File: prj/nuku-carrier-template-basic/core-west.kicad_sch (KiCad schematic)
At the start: 1 part, among them J4 DF40HC(4.0)-90DS-0.4V

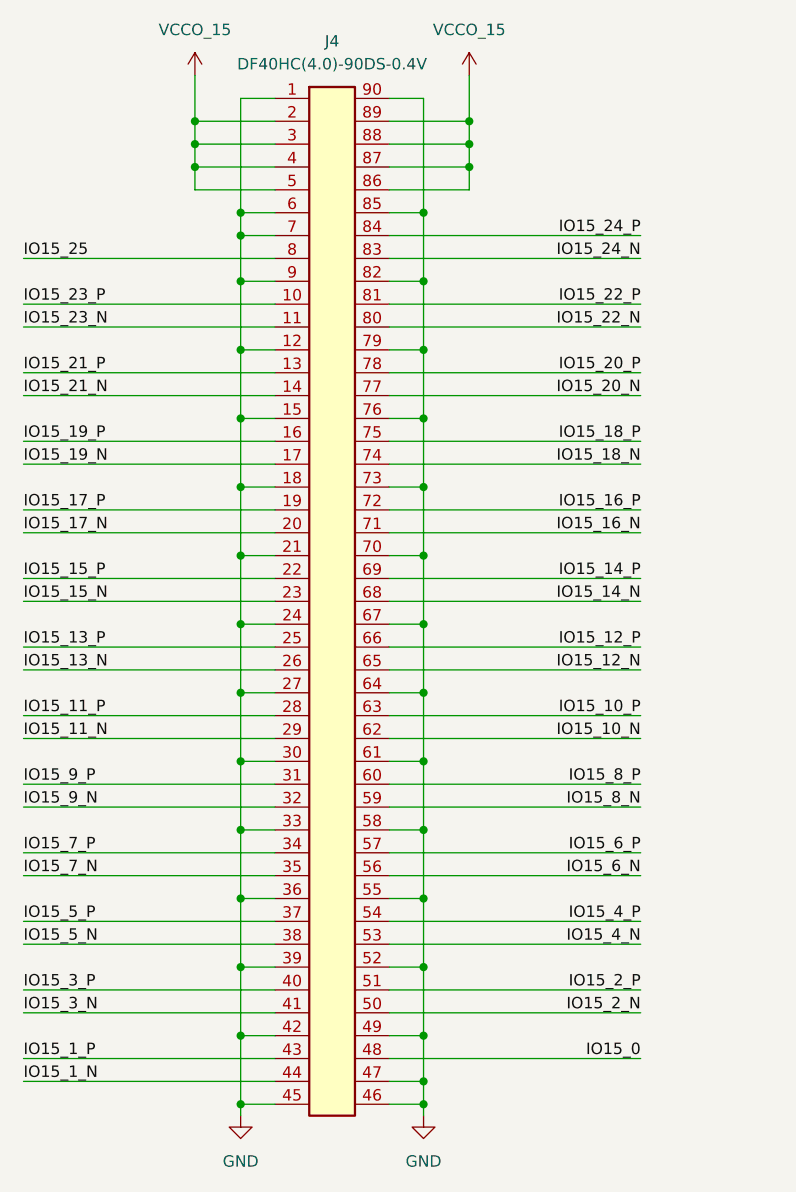
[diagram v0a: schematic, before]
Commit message: Finish template.basic + Production outputs
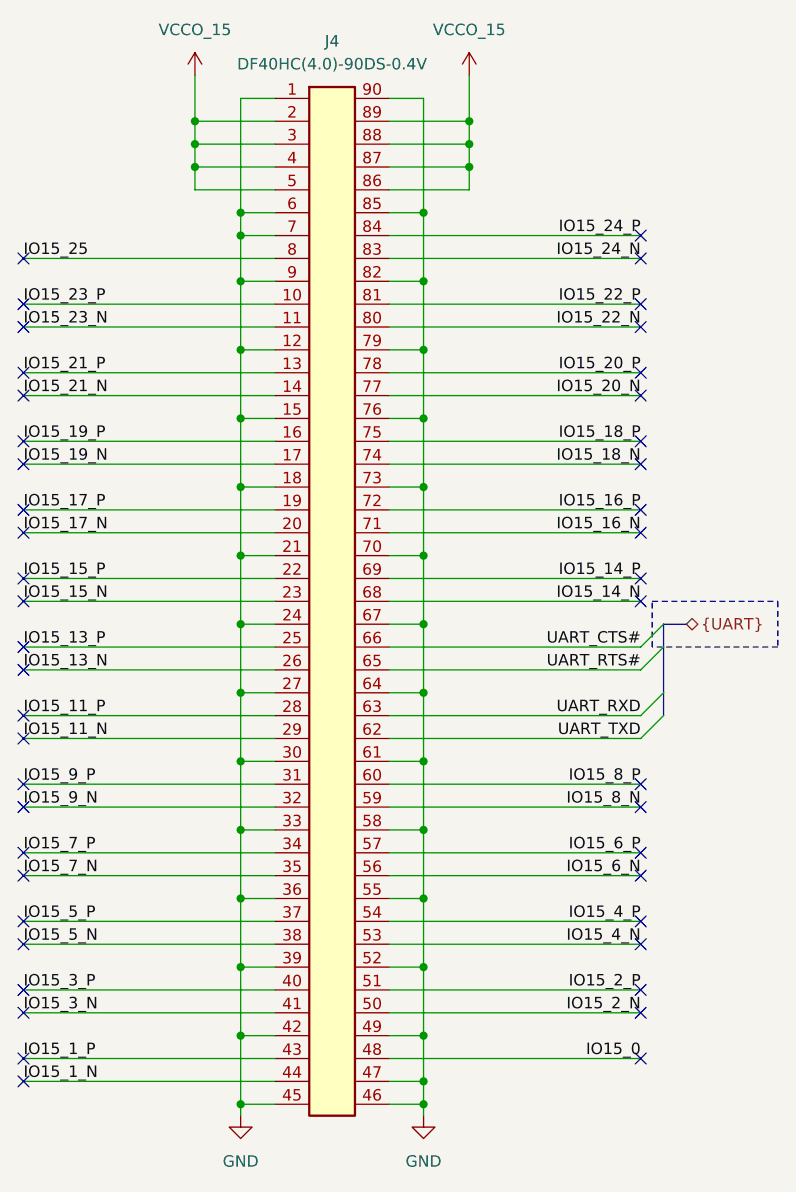
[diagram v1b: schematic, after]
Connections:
- net IO15_10_N renamed UART_TXD
- net IO15_10_P renamed UART_RXD
- net IO15_12_N renamed UART_RTS#
- net IO15_12_P renamed UART_CTS#
- no-connect marks 0 -> 46
